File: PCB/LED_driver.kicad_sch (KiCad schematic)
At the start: 14 parts, among them J4 LED 5050, Q3 UMW30N06, Q4 UMW30N06, Q5 UMW30N06, U7 MCP1416, U8 MCP1416

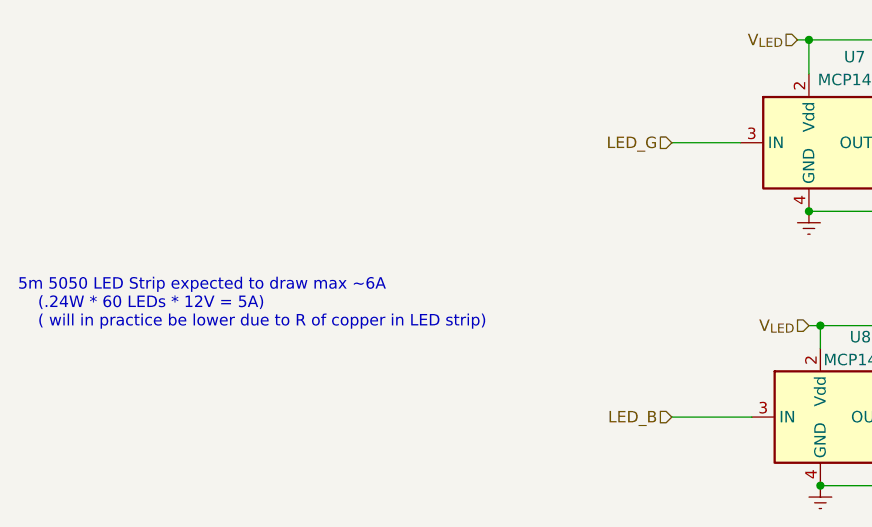
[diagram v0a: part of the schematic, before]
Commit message: changed mounting holes to ones without fiducials and fixed power calculation
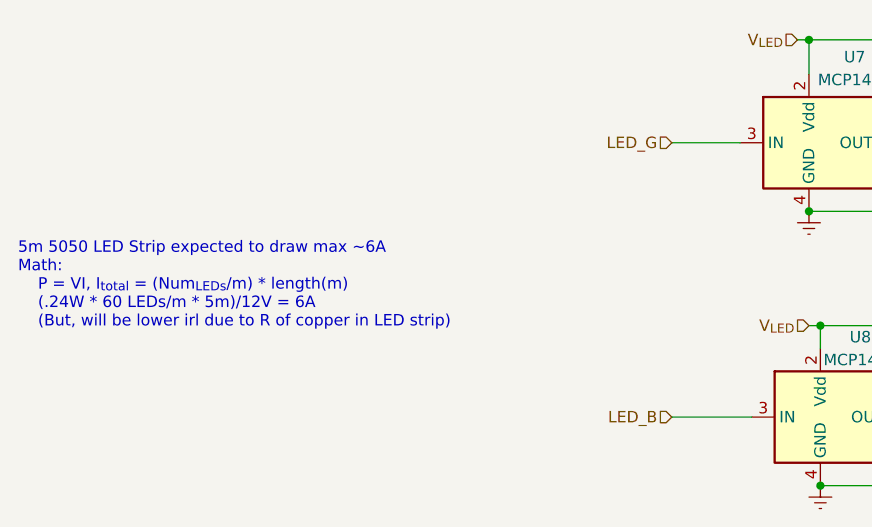
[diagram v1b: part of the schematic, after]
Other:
- note added: "5m 5050 LED Strip expected to draw max ~6A Math: P = VI, I_{total} = (Num_{LEDs}/m) * length(m) (.24W * 60 LEDs/m * 5m)/12V = 6A (But, will be lower irl due to R of copper in LED strip)"
- note removed: "5m 5050 LED Strip expected to draw max ~6A (.24W * 60 LEDs * 12V = 5A) ( will in practice be lower due to R of copper in LED strip)"
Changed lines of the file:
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@@
     (effects (font (size 1.27 1.27)) (justify left bottom))
   )
-  (text "5m 5050 LED Strip expected to draw max ~6A\n	(.24W * 60 LEDs * 12V = 5A)\n	( will in practice be lower due to R of copper in LED strip)"
+  (text "5m 5050 LED Strip expected to draw max ~6A\nMath: \n	P = VI, I_{total} = (Num_{LEDs}/m) * length(m)\n	(.24W * 60 LEDs/m * 5m)/12V = 6A\n	(But, will be lower irl due to R of copper in LED strip)"
     (at 25.781 98.806 0)
     (effects (font (size 1.27 1.27)) (justify left bottom))

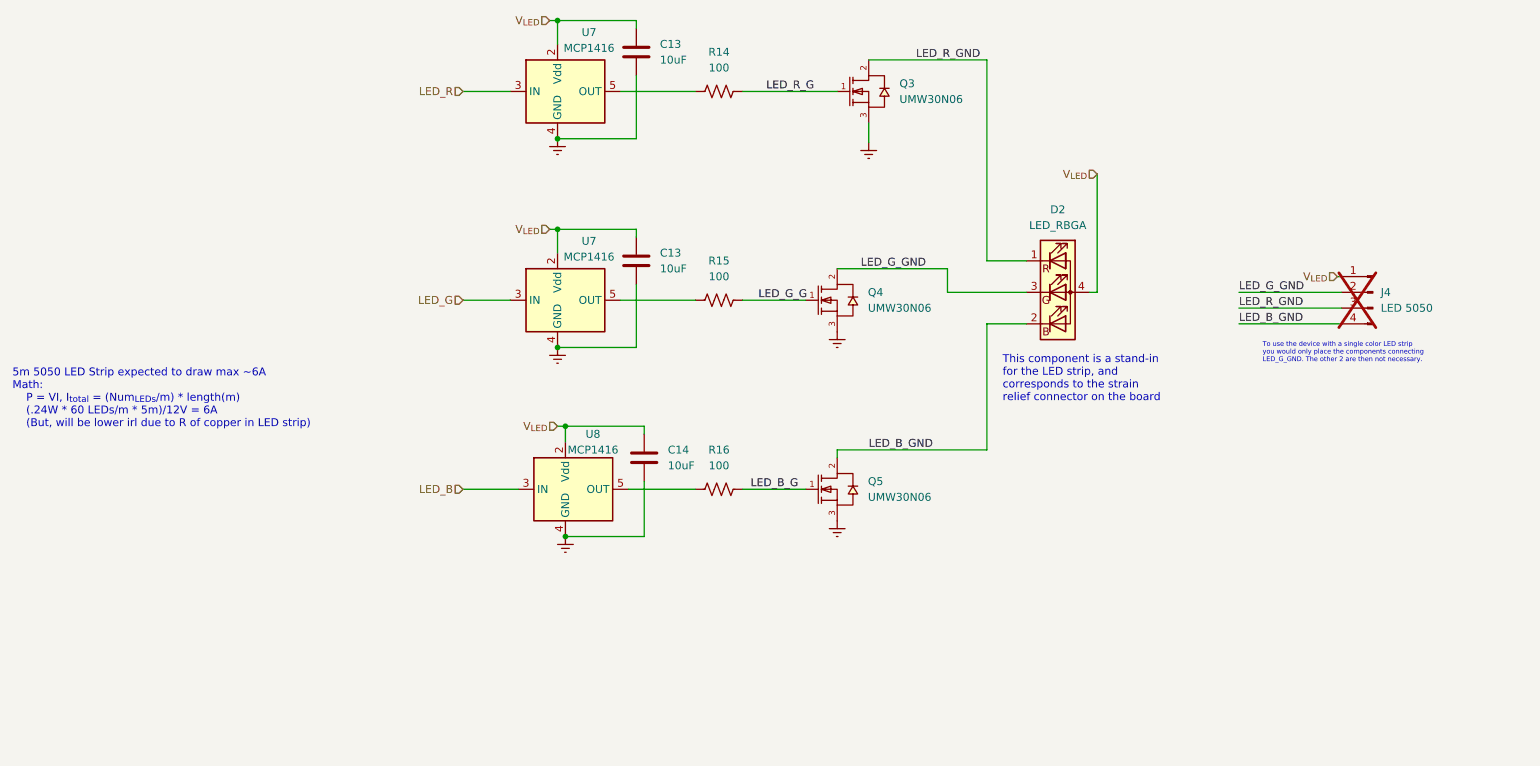
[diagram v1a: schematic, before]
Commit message: fuse added to schematic. began board re-layout
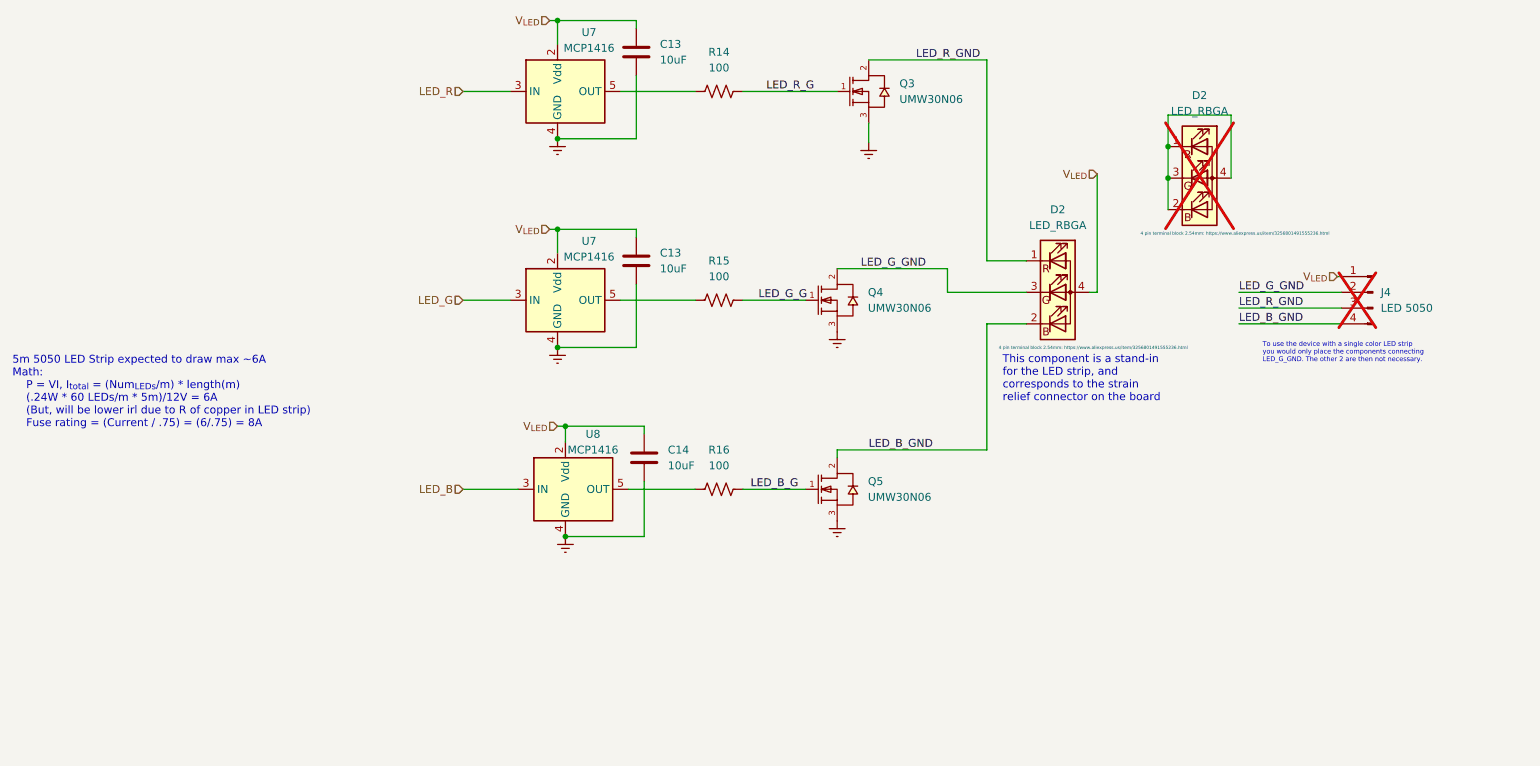
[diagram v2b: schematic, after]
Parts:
- added D2: LED_RBGA, Connector_Wire:SolderWire-0.15sqmm_1x04_P4mm_D0.5mm_OD1.5mm_Relief, symbol Device:LED_RBGA
- D2: footprint Connector_Wire:SolderWire-0.15sqmm_1x04_P4mm_D0.5mm_OD1.5mm_Relief -> TerminalBlock_Phoenix:TerminalBlock_Phoenix_MPT-0,5-4-2.54_1x04_P2.54mm_Horizontal; Note (none) -> 4 pin terminal block 2.54mm: https://www.aliexpress.us/item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
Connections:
- new net: D2.1 (RK), D2.2 (BK), D2.3 (GK), D2.4 (A)
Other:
- note added: "5m 5050 LED Strip expected to draw max ~6A Math: P = VI, I_{total} = (Num_{LEDs}/m) * length(m) (.24W * 60 LEDs/m * 5m)/12V = 6A (But, will be lower irl due to R of copper in LED strip) Fuse rating = (Current / .75) = (6/.75) = 8A"
- note removed: "5m 5050 LED Strip expected to draw max ~6A Math: P = VI, I_{total} = (Num_{LEDs}/m) * length(m) (.24W * 60 LEDs/m * 5m)/12V = 6A (But, will be lower irl due to R of copper in LED strip)"
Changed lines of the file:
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@@
     (comment 1 "jacobbokor.com")
   )
+  (junction (at 212.09 58.42) (diameter 0) (color 0 0 0 0)
+  )
   (junction (at 113.665 66.675) (diameter 0) (color 0 0 0 0)
   )
+  (junction (at 212.09 53.34) (diameter 0) (color 0 0 0 0)
+  )
   (junction (at 114.935 116.205) (diameter 0) (color 0 0 0 0)
   )
@@
     (stroke (width 0) (type default))
   )
+  (wire (pts (xy 212.09 58.42) (xy 212.09 63.5))
+    (stroke (width 0) (type default))
+  )
+  (wire (pts (xy 222.25 48.26) (xy 212.09 48.26))
+    (stroke (width 0) (type default))
+  )
   (wire (pts (xy 143.51 108.585) (xy 153.67 108.585))
     (stroke (width 0) (type default))
@@
     (stroke (width 0) (type default))
   )
+  (wire (pts (xy 212.09 48.26) (xy 212.09 53.34))
+    (stroke (width 0) (type default))
+  )
   (wire (pts (xy 223.52 76.835) (xy 240.03 76.835))
     (stroke (width 0) (type default))
@@
     (stroke (width 0) (type default))
   )
+  (wire (pts (xy 222.25 58.42) (xy 222.25 48.26))
+    (stroke (width 0) (type default))
+  )
   (wire (pts (xy 113.665 33.02) (xy 126.365 33.02))
     (stroke (width 0) (type default))
@@
   )
   (wire (pts (xy 112.395 66.675) (xy 113.665 66.675))
+    (stroke (width 0) (type default))
+  )
+  (wire (pts (xy 212.09 53.34) (xy 212.09 58.42))
     (stroke (width 0) (type default))
   )
@@
     (effects (font (size 1.27 1.27)) (justify left bottom))
   )
-  (text "5m 5050 LED Strip expected to draw max ~6A\nMath: \n	P = VI, I_{total} = (Num_{LEDs}/m) * length(m)\n	(.24W * 60 LEDs/m * 5m)/12V = 6A\n	(But, will be lower irl due to R of copper in LED strip)"
+  (text "5m 5050 LED Strip expected to draw max ~6A\nMath: \n	P = VI, I_{total} = (Num_{LEDs}/m) * length(m)\n	(.24W * 60 LEDs/m * 5m)/12V = 6A\n	(But, will be lower irl due to R of copper in LED strip)\n	Fuse rating = (Current / .75) = (6/.75) = 8A"
     (at 25.781 98.806 0)
     (effects (font (size 1.27 1.27)) (justify left bottom))
@@
     )
   )
+  (symbol (lib_id "Device:LED_RBGA") (at 217.17 58.42 0) (unit 1)
+    (in_bom no) (on_board no) (dnp yes) (fields_autoplaced)
+    (property "Reference" "D2" (at 217.17 45.085 0)
+      (effects (font (size 1.27 1.27)))
+    )
+    (property "Value" "LED_RBGA" (at 217.17 47.625 0)
+      (effects (font (size 1.27 1.27)))
+    )
+    (property "Footprint" "Connector_Wire:SolderWire-0.15sqmm_1x04_P4mm_D0.5mm_OD1.5mm_Relief" (at 217.17 59.69 0)
+      (effects (font (size 1.27 1.27)) hide)
+    )
+    (property "Datasheet" "~" (at 217.17 59.69 0)
+      (effects (font (size 1.27 1.27)) hide)
+    )
+    (property "Note" "4 pin terminal block 2.54mm: https://www.aliexpress.us/item/3256801491555236.html" (at 222.885 67.31 0)
+      (effects (font (size 0.508 0.508)))
+    )
+    (property "Sim.Enable" "0" (at 217.17 58.42 0)
+      (effects (font (size 1.27 1.27)) hide)
+    )
+    (pin "1")
+    (pin "2")
+    (pin "3")
+    (pin "4")
+    (instances
+      (project "iot_led_strip_pcb"
+        (path "/745f5767-ebad-4719-b66e-073bc90db4bc/af18acc8-a8c3-4e1e-8a57-49b565af3262"
+          (reference "D2") (unit 1)
+        )
+      )
+      (project "dumb-led-driver"
+        (path "/b6358773-9a18-4eb2-bc1b-d38393a8df39/906d9b01-c5b2-4615-86e8-3c8294737d59"
+          (reference "D4") (unit 1)
+        )
+      )
+      (project "LED_driver"
+        (path "/dc96e041-5ba7-4eeb-baa0-ca65355a480c"
+          (reference "D2") (unit 1)
+        )
+      )
+    )
+  )
   (symbol (lib_id "Device:R_US") (at 139.7 78.105 90) (unit 1)
     (in_bom yes) (on_board yes) (dnp no) (fields_autoplaced)
@@
       (effects (font (size 1.27 1.27)))
     )
-    (property "Footprint" "Connector_Wire:SolderWire-0.15sqmm_1x04_P4mm_D0.5mm_OD1.5mm_Relief" (at 194.31 78.105 0)
+    (property "Footprint" "TerminalBlock_Phoenix:TerminalBlock_Phoenix_MPT-0,5-4-2.54_1x04_P2.54mm_Horizontal" (at 194.31 78.105 0)
       (effects (font (size 1.27 1.27)) hide)
     )
@@
       (effects (font (size 1.27 1.27)) hide)
     )
-    (property "Note" "" (at 200.025 85.725 0)
+    (property "Note" "4 pin terminal block 2.54mm: https://www.aliexpress.us/item/3256801491555236.html" (at 200.025 85.725 0)
       (effects (font (size 0.508 0.508)))
     )

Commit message: began rev2 of layout. board size will have to be increased
- will need to make compomises regarding I/O, wont be able to make both power in and out fit on same short side :(
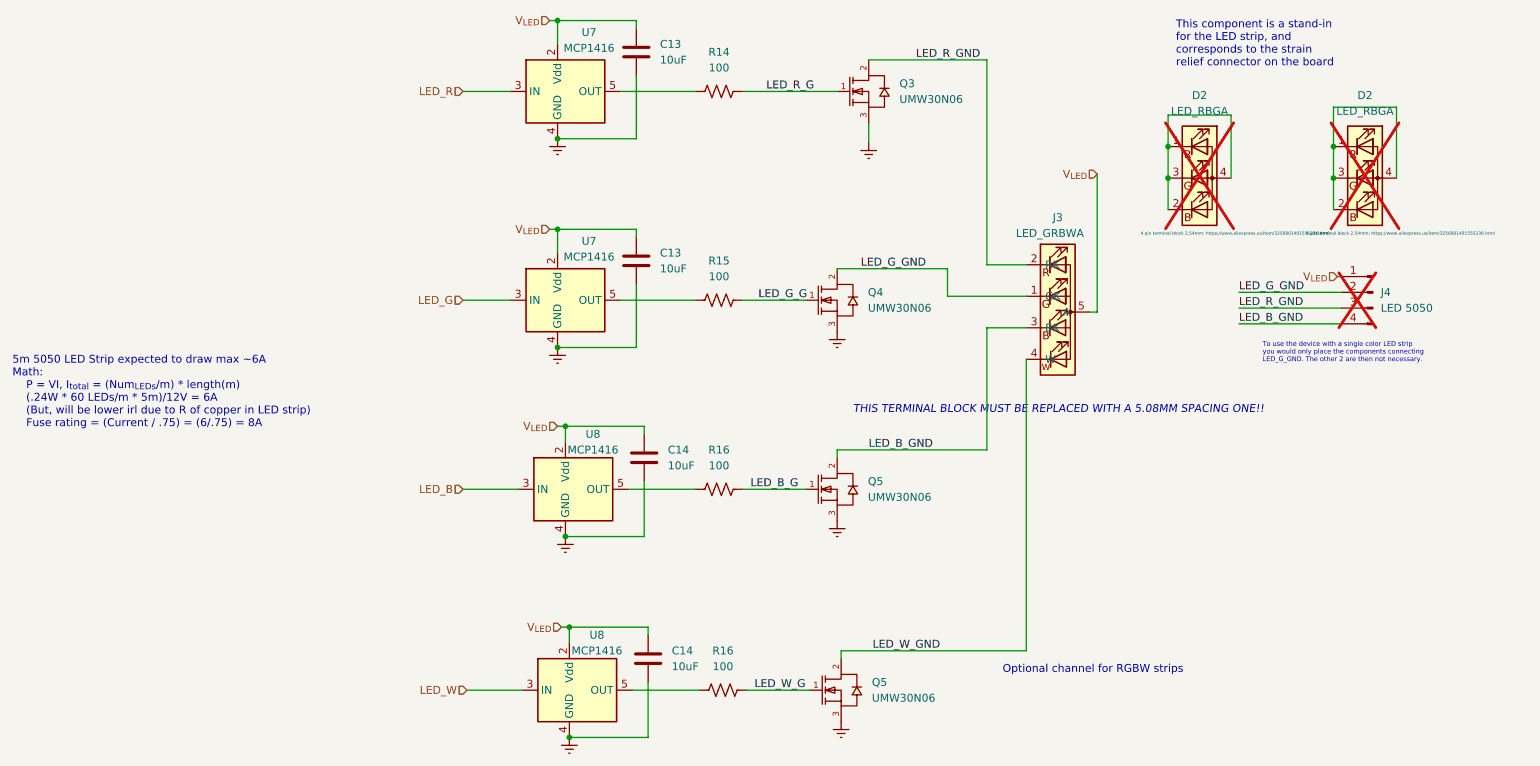
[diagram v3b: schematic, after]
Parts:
- added C14: 10uF, Capacitor_SMD:C_0805_2012Metric_Pad1.18x1.45mm_HandSolder, symbol Device:C
- added J3: LED_GRBWA, TerminalBlock_Phoenix:TerminalBlock_Phoenix_MPT-0,5-5-2.54_1x05_P2.54mm_Horizontal, symbol projectlib:LED_GRBWA
- added Q5: UMW30N06, Package_TO_SOT_SMD:TO-252-2, symbol UMW30N06:UMW30N06
- added R16: 100, Resistor_SMD:R_0805_2012Metric_Pad1.20x1.40mm_HandSolder, symbol Device:R_US
- added U8: MCP1416, Package_TO_SOT_SMD:SOT-23-5_HandSoldering, symbol Driver_FET:MCP1416
- D2: now not fitted
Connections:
- net Earth: now also C14.2, Q5.3 (S), U8.4 (GND)
- net LED_B_GND: now also J3.3 (BK); no longer D2.2 (BK)
- net LED_G_GND: now also J3.1 (GK); no longer D2.3 (GK)
- net LED_R_GND: now also J3.2 (RK); no longer D2.1 (RK)
- net V_{LED}: now also C14.1, J3.5 (A), U8.2 (Vdd); no longer D2.4 (A)
- new net: R16.1, U8.5 (OUT)
- new net: D2.1 (RK), D2.2 (BK), D2.3 (GK), D2.4 (A)
- new net LED_W: U8.3 (IN)
- new net LED_W_G: Q5.1 (G), R16.2
- new net LED_W_GND: J3.4 (W), Q5.2 (D)
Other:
- note added: "Optional channel for RGBW strips"
- note added: "THIS TERMINAL BLOCK MUST BE REPLACED WITH A 5.08MM SPACING ONE!!"
